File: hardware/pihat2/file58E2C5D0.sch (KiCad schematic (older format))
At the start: 43 parts, among them P1 USB_OTG, P2 BATT, P3 THERM, U1 MCP73833, U2 SMA_Edge_Mount, U3 SMA_Edge_Mount, U4 TPS61027, U5 MCP3021, U6 Si4464, X1 30MHz

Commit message: Worked on RF Layout.
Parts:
- removed C2: 10uF, Capacitors_SMD:C_0805, symbol C
- removed X1: 30MHz, Crystals:Crystal_SMD_5032_4Pads, symbol CRYSTAL_SMD
- added C10, C13: C, Capacitors_SMD:C_0805, symbol C
- added Y1: Crystal, Crystals:Crystal_HC49-SD_SMD, symbol Crystal
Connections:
- wire segments 164 -> 167

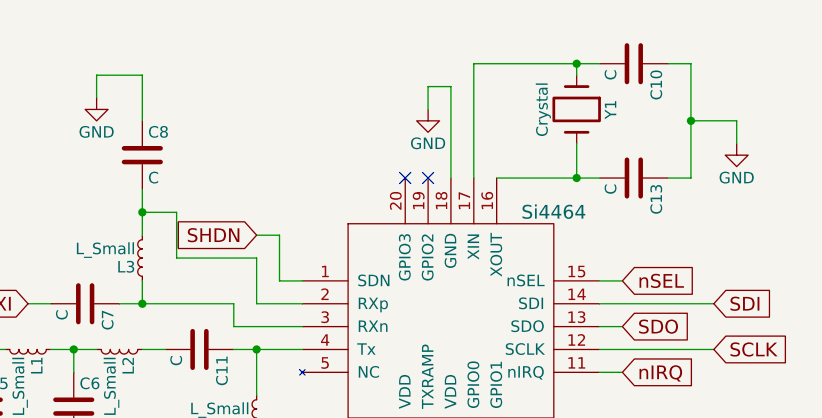
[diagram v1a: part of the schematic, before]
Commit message: Minor changes to pihat 2 in prep for boardhouse #2.
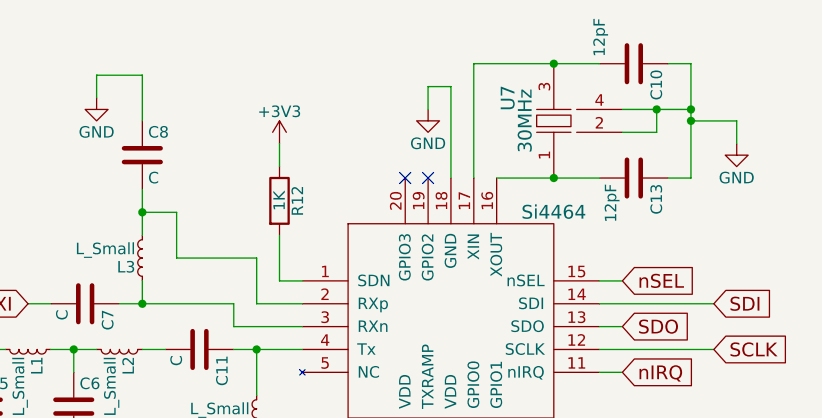
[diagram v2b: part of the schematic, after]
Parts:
- removed Y1: Crystal, Crystals:Crystal_HC49-SD_SMD, symbol Crystal
- added R12: 1K, Resistors_SMD:R_0805, symbol R
- added U7: 30MHz, Crystals:Crystal_SMD_Abracon_ABM3C-4pin_5.0x3.2mm, symbol AM3B_CRYSTAL
- C10, C13: value C -> 12pF
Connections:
- net labels removed: SHDN
- wire segments 167 -> 168
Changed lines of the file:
@@
 EESchema Schematic File Version 2
+LIBS:RPi_Hat-rescue
 LIBS:power
 LIBS:device
@@
 LIBS:contrib
 LIBS:valves
-LIBS:RFT
 LIBS:RPi_Hat-cache
 EELAYER 25 0
@@
 	9000 1600 9000 1400
 Wire Wire Line
-	9000 1400 8900 1400
-Text GLabel 8900 1400 0    60   Input ~ 0
-SHDN
-Wire Wire Line
 	9100 1900 8800 1900
 $Comp
@@
 	8200 4300 8200 4400
 $Comp
-L GND #PWR025
+L GND #PWR024
 U 1 1 58E2C8DB
 P 8200 4400
-F 0 "#PWR025" H 8200 4150 50  0001 C CNN
+F 0 "#PWR024" H 8200 4150 50  0001 C CNN
 F 1 "GND" H 8200 4250 50  0000 C CNN
 F 2 "" H 8200 4400 50  0000 C CNN
@@
 	9600 3300 9600 3400
 $Comp
-L GND #PWR026
+L GND #PWR025
 U 1 1 58E2C8DC
 P 9600 3400
-F 0 "#PWR026" H 9600 3150 50  0001 C CNN
+F 0 "#PWR025" H 9600 3150 50  0001 C CNN
 F 1 "GND" H 9600 3250 50  0000 C CNN
 F 2 "" H 9600 3400 50  0000 C CNN
@@
 	6950 3400 6950 3500
 $Comp
-L GND #PWR027
+L GND #PWR026
 U 1 1 58E2C8E0
 P 6950 3500
-F 0 "#PWR027" H 6950 3250 50  0001 C CNN
+F 0 "#PWR026" H 6950 3250 50  0001 C CNN
 F 1 "GND" H 6950 3350 50  0000 C CNN
 F 2 "" H 6950 3500 50  0000 C CNN
@@
 	7500 4600 7500 4700
 $Comp
-L GND #PWR028
+L GND #PWR027
 U 1 1 58E2C8E3
 P 7500 4700
-F 0 "#PWR028" H 7500 4450 50  0001 C CNN
+F 0 "#PWR027" H 7500 4450 50  0001 C CNN
 F 1 "GND" H 7500 4550 50  0000 C CNN
 F 2 "" H 7500 4700 50  0000 C CNN
@@
 	10550 3900 10550 4000
 $Comp
-L GND #PWR029
+L GND #PWR028
 U 1 1 58E2C8E5
 P 10550 4000
-F 0 "#PWR029" H 10550 3750 50  0001 C CNN
+F 0 "#PWR028" H 10550 3750 50  0001 C CNN
 F 1 "GND" H 10550 3850 50  0000 C CNN
 F 2 "" H 10550 4000 50  0000 C CNN
@@
 	10900 4400 10900 4500
 $Comp
-L GND #PWR030
+L GND #PWR029
 U 1 1 58E2C8E8
 P 10900 4500
-F 0 "#PWR030" H 10900 4250 50  0001 C CNN
+F 0 "#PWR029" H 10900 4250 50  0001 C CNN
 F 1 "GND" H 10900 4350 50  0000 C CNN
 F 2 "" H 10900 4500 50  0000 C CNN
@@
 Connection ~ 8650 5250
 $Comp
-L GND #PWR031
+L GND #PWR030
 U 1 1 58E2C8EB
 P 8650 5350
-F 0 "#PWR031" H 8650 5100 50  0001 C CNN
+F 0 "#PWR030" H 8650 5100 50  0001 C CNN
 F 1 "GND" H 8650 5200 50  0000 C CNN
 F 2 "" H 8650 5350 50  0000 C CNN
@@
 	8900 4750 8900 4650
 $Comp
-L +5V #PWR032
+L +5V #PWR031
 U 1 1 58E2C8EC
 P 8900 4650
-F 0 "#PWR032" H 8900 4500 50  0001 C CNN
+F 0 "#PWR031" H 8900 4500 50  0001 C CNN
 F 1 "+5V" H 8900 4790 50  0000 C CNN
 F 2 "" H 8900 4650 50  0000 C CNN
@@
 	6550 6550 6950 6550
 $Comp
-L +5V #PWR033
+L +5V #PWR032
 U 1 1 58E2C8F6
 P 1500 6150
-F 0 "#PWR033" H 1500 6000 50  0001 C CNN
+F 0 "#PWR032" H 1500 6000 50  0001 C CNN
 F 1 "+5V" H 1500 6290 50  0000 C CNN
 F 2 "" H 1500 6150 50  0000 C CNN
@@
 $EndComp
 $Comp
-L GND #PWR034
+L GND #PWR033
 U 1 1 58E2C8F7
 P 1500 6650
-F 0 "#PWR034" H 1500 6400 50  0001 C CNN
+F 0 "#PWR033" H 1500 6400 50  0001 C CNN
 F 1 "GND" H 1500 6500 50  0000 C CNN
 F 2 "" H 1500 6650 50  0000 C CNN
@@
 	3100 6500 3100 6600
 $Comp
-L GND #PWR035
+L GND #PWR034
 U 1 1 58E2C8F9
 P 3100 6600
-F 0 "#PWR035" H 3100 6350 50  0001 C CNN
+F 0 "#PWR034" H 3100 6350 50  0001 C CNN
 F 1 "GND" H 3100 6450 50  0000 C CNN
 F 2 "" H 3100 6600 50  0000 C CNN
@@
 Connection ~ 10550 2550
 $Comp
-L GND #PWR036
+L GND #PWR035
 U 1 1 58E2C901
 P 10650 2550
-F 0 "#PWR036" H 10650 2300 50  0001 C CNN
+F 0 "#PWR035" H 10650 2300 50  0001 C CNN
 F 1 "GND" H 10650 2400 50  0000 C CNN
 F 2 "" H 10650 2550 50  0000 C CNN
@@
 	2250 950  2250 850
 $Comp
-L +5V #PWR037
+L +5V #PWR036
 U 1 1 58E30706
 P 2250 850
-F 0 "#PWR037" H 2250 700 50  0001 C CNN
+F 0 "#PWR036" H 2250 700 50  0001 C CNN
 F 1 "+5V" H 2250 990 50  0000 C CNN
 F 2 "" H 2250 850 50  0000 C CNN
@@
 	2250 1850 2250 1950
 $Comp
-L GND #PWR038
+L GND #PWR037
 U 1 1 58E3098E
 P 2250 1950
-F 0 "#PWR038" H 2250 1700 50  0001 C CNN
+F 0 "#PWR037" H 2250 1700 50  0001 C CNN
 F 1 "GND" H 2250 1800 50  0000 C CNN
 F 2 "" H 2250 1950 50  0000 C CNN
@@
 VBATFILT
 $Comp
-L Crystal Y1
-U 1 1 58F13A4E
-P 10300 850
-F 0 "Y1" H 10300 1000 50  0000 C CNN
-F 1 "Crystal" H 10300 700 50  0000 C CNN
-F 2 "Crystals:Crystal_HC49-SD_SMD" H 10300 850 50  0001 C CNN
-F 3 "" H 10300 850 50  0000 C CNN
-	1    10300 850
-	0    1    1    0
-$EndComp
-Wire Wire Line
-	9850 650  10400 650
-Wire Wire Line
-	10300 650  10300 700
-Wire Wire Line
-	9950 1150 10400 1150
-Wire Wire Line
-	10300 1150 10300 1000
-$Comp
 L C C10
 U 1 1 58F142C3
 P 10550 650
 F 0 "C10" H 10575 750 50  0000 L CNN
-F 1 "C" H 10575 550 50  0000 L CNN
+F 1 "12pF" H 10350 500 50  0000 L CNN
 F 2 "Capacitors_SMD:C_0805" H 10588 500 50  0001 C CNN
 F 3 "" H 10550 650 50  0000 C CNN
@@
 	0    1    1    0
 $EndComp
-Connection ~ 10300 650
-Connection ~ 10300 1150
 $Comp
 L C C13
@@
 P 10550 1150
 F 0 "C13" H 10575 1250 50  0000 L CNN
-F 1 "C" H 10575 1050 50  0000 L CNN
+F 1 "12pF" H 10575 1050 50  0000 L CNN
 F 2 "Capacitors_SMD:C_0805" H 10588 1000 50  0001 C CNN
 F 3 "" H 10550 1150 50  0000 C CNN
@@
 Connection ~ 10800 900
 $Comp
-L GND #PWR039
+L GND #PWR038
 U 1 1 58F147CE
 P 11000 1000
-F 0 "#PWR039" H 11000 750 50  0001 C CNN
+F 0 "#PWR038" H 11000 750 50  0001 C CNN
 F 1 "GND" H 11000 850 50  0000 C CNN
 F 2 "" H 11000 1000 50  0000 C CNN
@@
 	1    0    0    -1
 $EndComp
+Wire Wire Line
+	10650 850  10650 950
+Wire Wire Line
+	10500 850  10800 850
+Connection ~ 10800 850
+$Comp
+L R R12
+U 1 1 59011587
+P 9000 1250
+F 0 "R12" V 9080 1250 50  0000 C CNN
+F 1 "1K" V 9000 1250 50  0000 C CNN
+F 2 "Resistors_SMD:R_0805" V 8930 1250 50  0001 C CNN
+F 3 "" H 9000 1250 50  0000 C CNN
+	1    9000 1250
+	1    0    0    -1
+$EndComp
+Wire Wire Line
+	9000 1100 9000 1000
+$Comp
+L +3V3 #PWR039
+U 1 1 59011701
+P 9000 1000
+F 0 "#PWR039" H 9000 850 50  0001 C CNN
+F 1 "+3V3" H 9000 1140 50  0000 C CNN
+F 2 "" H 9000 1000 50  0000 C CNN
+F 3 "" H 9000 1000 50  0000 C CNN
+	1    9000 1000
+	1    0    0    -1
+$EndComp
+$Comp
+L AM3B_CRYSTAL U7
+U 1 1 59011E68
+P 10200 900
+F 0 "U7" H 10300 1100 60  0000 C CNN
+F 1 "30MHz" H 10200 1025 60  0000 C CNN
+F 2 "Crystals:Crystal_SMD_Abracon_ABM3C-4pin_5.0x3.2mm" H 10200 900 60  0001 C CNN
+F 3 "" H 10200 900 60  0001 C CNN
+	1    10200 900
+	0    -1   -1   0
+$EndComp
+Wire Wire Line
+	9850 650  10400 650
+Connection ~ 10200 650
+Wire Wire Line
+	9950 1150 10400 1150
+Connection ~ 10200 1150
+Connection ~ 10650 850
+Wire Wire Line
+	10650 950  10500 950
 $EndSCHEMATC

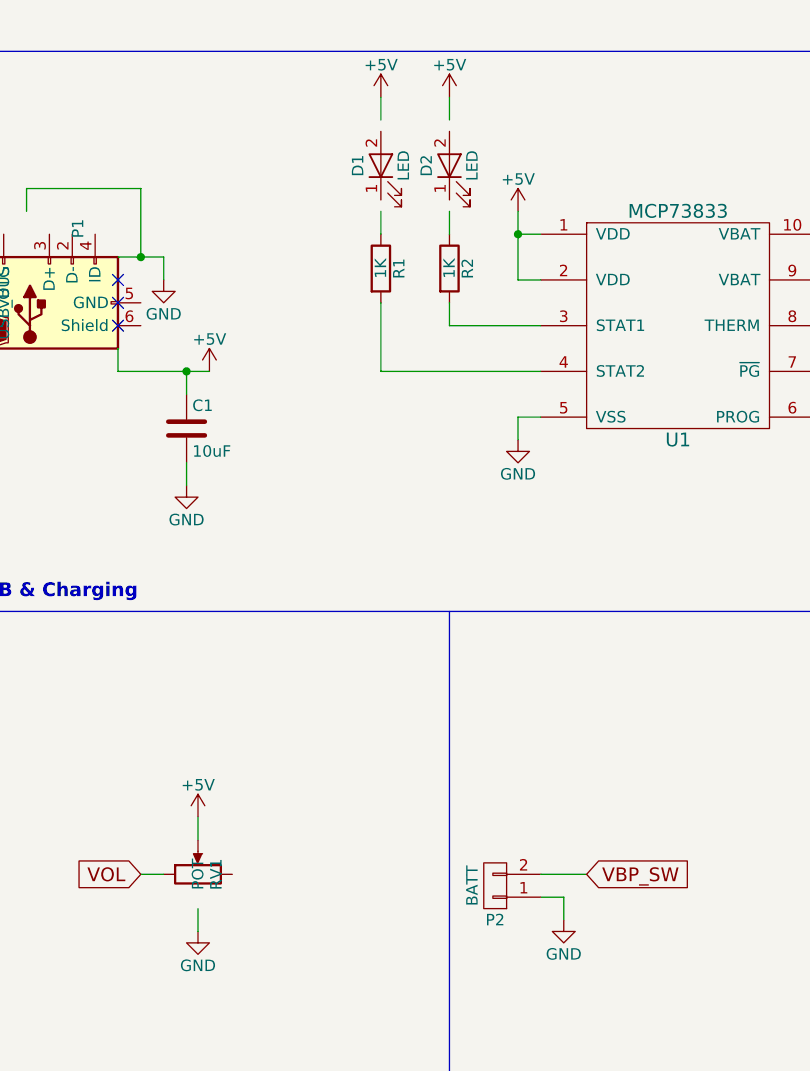
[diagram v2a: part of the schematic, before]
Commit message: Fixed issues with grounding and trace size.
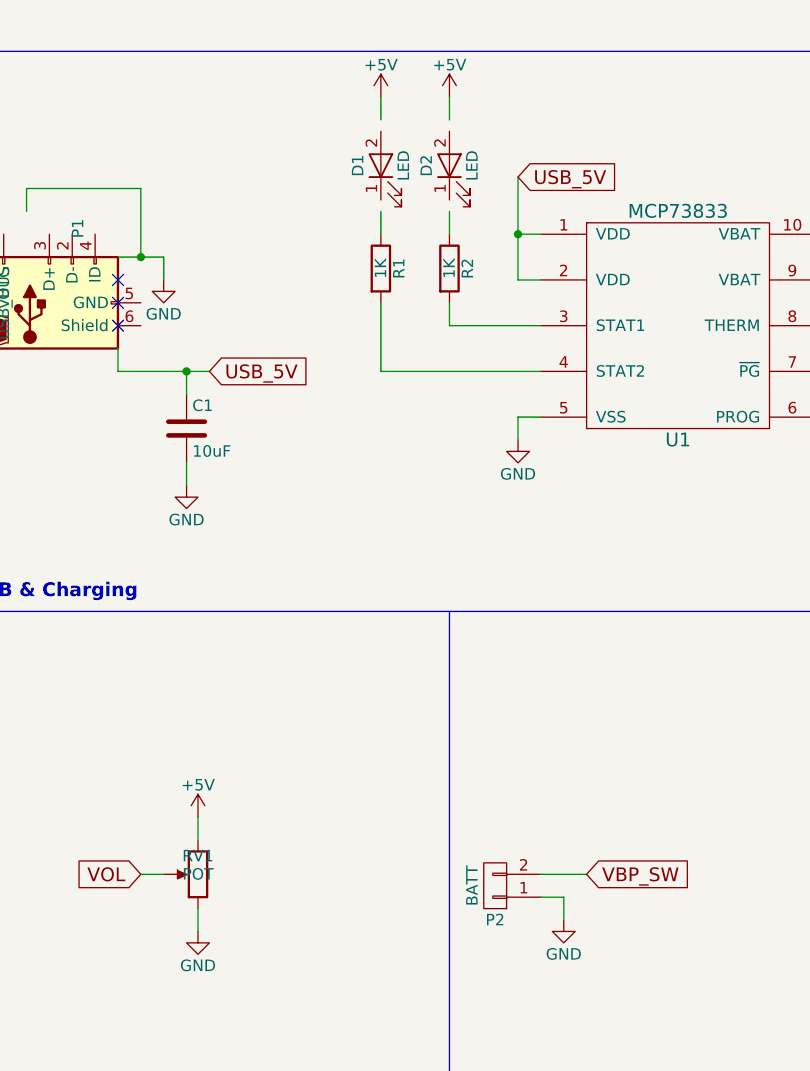
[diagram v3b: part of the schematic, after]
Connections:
- net labels added: USB_5V
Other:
- moved on the sheet: RV1
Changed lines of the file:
@@
 LIBS:contrib
 LIBS:valves
+LIBS:RFT
 LIBS:RPi_Hat-cache
 EELAYER 25 0
@@
 $EndComp
 Connection ~ 1450 4200
-$Comp
-L +5V #PWR016
-U 1 1 58E2C8C5
-P 1550 4200
-F 0 "#PWR016" H 1550 4050 50  0001 C CNN
-F 1 "+5V" H 1550 4340 50  0000 C CNN
-F 2 "" H 1550 4200 50  0000 C CNN
-F 3 "" H 1550 4200 50  0000 C CNN
-	1    1550 4200
-	1    0    0    -1
-$EndComp
 Wire Bus Line
 	500  2800 4300 2800
@@
 $EndComp
 Wire Wire Line
-	3000 3800 2900 3800
-Wire Wire Line
-	2900 3800 2900 3500
+	2900 3800 3000 3800
+Wire Wire Line
+	2900 3350 2900 3800
 Wire Wire Line
 	3000 3600 2900 3600
 Connection ~ 2900 3600
 $Comp
-L +5V #PWR017
-U 1 1 58E2C8C7
-P 2900 3500
-F 0 "#PWR017" H 2900 3350 50  0001 C CNN
-F 1 "+5V" H 2900 3640 50  0000 C CNN
-F 2 "" H 2900 3500 50  0000 C CNN
-F 3 "" H 2900 3500 50  0000 C CNN
-	1    2900 3500
-	1    0    0    -1
-$EndComp
-$Comp
-L +5V #PWR018
+L +5V #PWR016
 U 1 1 58E2C8C8
 P 2600 3000
-F 0 "#PWR018" H 2600 2850 50  0001 C CNN
+F 0 "#PWR016" H 2600 2850 50  0001 C CNN
 F 1 "+5V" H 2600 3140 50  0000 C CNN
 F 2 "" H 2600 3000 50  0000 C CNN
@@
 $EndComp
 $Comp
-L +5V #PWR019
+L +5V #PWR017
 U 1 1 58E2C8C9
 P 2300 3000
-F 0 "#PWR019" H 2300 2850 50  0001 C CNN
+F 0 "#PWR017" H 2300 2850 50  0001 C CNN
 F 1 "+5V" H 2300 3140 50  0000 C CNN
 F 2 "" H 2300 3000 50  0000 C CNN
@@
 U 1 1 58E2C8CB
 P 2600 3300
+AR Path="/58E2C8CB" Ref="D2"  Part="1"
+AR Path="/5515D395/58E2C5D1/58E2C8CB" Ref="D2"  Part="1"
 F 0 "D2" H 2600 3400 50  0000 C CNN
 F 1 "LED" H 2600 3200 50  0000 C CNN
@@
 U 1 1 58E2C8CD
 P 2300 3300
+AR Path="/58E2C8CD" Ref="D1"  Part="1"
+AR Path="/5515D395/58E2C5D1/58E2C8CD" Ref="D1"  Part="1"
 F 0 "D1" H 2300 3400 50  0000 C CNN
 F 1 "LED" H 2300 3200 50  0000 C CNN
@@
 	2900 4400 2900 4500
 $Comp
-L GND #PWR020
+L GND #PWR018
 U 1 1 58E2C8CE
 P 2900 4500
-F 0 "#PWR020" H 2900 4250 50  0001 C CNN
+F 0 "#PWR018" H 2900 4250 50  0001 C CNN
 F 1 "GND" H 2900 4350 50  0000 C CNN
 F 2 "" H 2900 4500 50  0000 C CNN
@@
 	4300 4800 4300 4900
 $Comp
-L GND #PWR021
+L GND #PWR019
 U 1 1 58E2C8D0
 P 4300 4900
-F 0 "#PWR021" H 4300 4650 50  0001 C CNN
+F 0 "#PWR019" H 4300 4650 50  0001 C CNN
 F 1 "GND" H 4300 4750 50  0000 C CNN
 F 2 "" H 4300 4900 50  0000 C CNN
@@
 U 1 1 58E2C8D2
 P 4600 2800
+AR Path="/58E2C8D2" Ref="D3"  Part="1"
+AR Path="/5515D395/58E2C5D1/58E2C8D2" Ref="D3"  Part="1"
 F 0 "D3" H 4600 2900 50  0000 C CNN
 F 1 "LED" H 4600 2700 50  0000 C CNN
@@
 $EndComp
 $Comp
-L +5V #PWR022
+L +5V #PWR020
 U 1 1 58E2C8D3
 P 4600 2500
-F 0 "#PWR022" H 4600 2350 50  0001 C CNN
+F 0 "#PWR020" H 4600 2350 50  0001 C CNN
 F 1 "+5V" H 4600 2640 50  0000 C CNN
 F 2 "" H 4600 2500 50  0000 C CNN
@@
 Connection ~ 5200 4900
 $Comp
-L GND #PWR023
+L GND #PWR021
 U 1 1 58E2C8D7
 P 5200 5000
-F 0 "#PWR023" H 5200 4750 50  0001 C CNN
+F 0 "#PWR021" H 5200 4750 50  0001 C CNN
 F 1 "GND" H 5200 4850 50  0000 C CNN
 F 2 "" H 5200 5000 50  0000 C CNN
@@
 	8200 4300 8200 4400
 $Comp
-L GND #PWR024
+L GND #PWR022
 U 1 1 58E2C8DB
 P 8200 4400
-F 0 "#PWR024" H 8200 4150 50  0001 C CNN
+F 0 "#PWR022" H 8200 4150 50  0001 C CNN
 F 1 "GND" H 8200 4250 50  0000 C CNN
 F 2 "" H 8200 4400 50  0000 C CNN
@@
 	9600 3300 9600 3400
 $Comp
-L GND #PWR025
+L GND #PWR023
 U 1 1 58E2C8DC
 P 9600 3400
-F 0 "#PWR025" H 9600 3150 50  0001 C CNN
+F 0 "#PWR023" H 9600 3150 50  0001 C CNN
 F 1 "GND" H 9600 3250 50  0000 C CNN
 F 2 "" H 9600 3400 50  0000 C CNN
@@
 	6950 3400 6950 3500
 $Comp
-L GND #PWR026
+L GND #PWR024
 U 1 1 58E2C8E0
 P 6950 3500
-F 0 "#PWR026" H 6950 3250 50  0001 C CNN
+F 0 "#PWR024" H 6950 3250 50  0001 C CNN
 F 1 "GND" H 6950 3350 50  0000 C CNN
 F 2 "" H 6950 3500 50  0000 C CNN
@@
 Wire Wire Line
 	7400 3700 8300 3700
-$Comp
-L R R7
-U 1 1 58E2C8E1
-P 7500 3950
-F 0 "R7" V 7580 3950 50  0000 C CNN
-F 1 "R" V 7500 3950 50  0000 C CNN
-F 2 "Resistors_SMD:R_0603" V 7430 3950 50  0001 C CNN
-F 3 "" H 7500 3950 50  0000 C CNN
-	1    7500 3950
-	1    0    0    -1
-$EndComp
 $Comp
 L R R8
@@
 	7500 4600 7500 4700
 $Comp
-L GND #PWR027
+L GND #PWR025
 U 1 1 58E2C8E3
 P 7500 4700
-F 0 "#PWR027" H 7500 4450 50  0001 C CNN
+F 0 "#PWR025" H 7500 4450 50  0001 C CNN
 F 1 "GND" H 7500 4550 50  0000 C CNN
 F 2 "" H 7500 4700 50  0000 C CNN
@@
 	10550 3900 10550 4000
 $Comp
-L GND #PWR028
+L GND #PWR026
 U 1 1 58E2C8E5
 P 10550 4000
-F 0 "#PWR028" H 10550 3750 50  0001 C CNN
+F 0 "#PWR026" H 10550 3750 50  0001 C CNN
 F 1 "GND" H 10550 3850 50  0000 C CNN
 F 2 "" H 10550 4000 50  0000 C CNN
@@
 	10900 4400 10900 4500
 $Comp
-L GND #PWR029
+L GND #PWR027
 U 1 1 58E2C8E8
 P 10900 4500
-F 0 "#PWR029" H 10900 4250 50  0001 C CNN
+F 0 "#PWR027" H 10900 4250 50  0001 C CNN
 F 1 "GND" H 10900 4350 50  0000 C CNN
 F 2 "" H 10900 4500 50  0000 C CNN
@@
 Connection ~ 8650 5250
 $Comp
-L GND #PWR030
+L GND #PWR028
 U 1 1 58E2C8EB
 P 8650 5350
-F 0 "#PWR030" H 8650 5100 50  0001 C CNN
+F 0 "#PWR028" H 8650 5100 50  0001 C CNN
 F 1 "GND" H 8650 5200 50  0000 C CNN
 F 2 "" H 8650 5350 50  0000 C CNN
@@
 	8900 4750 8900 4650
 $Comp
-L +5V #PWR031
+L +5V #PWR029
 U 1 1 58E2C8EC
 P 8900 4650
-F 0 "#PWR031" H 8900 4500 50  0001 C CNN
+F 0 "#PWR029" H 8900 4500 50  0001 C CNN
 F 1 "+5V" H 8900 4790 50  0000 C CNN
 F 2 "" H 8900 4650 50  0000 C CNN
@@
 	6550 6550 6950 6550
 $Comp
-L +5V #PWR032
+L +5V #PWR030
 U 1 1 58E2C8F6
 P 1500 6150
-F 0 "#PWR032" H 1500 6000 50  0001 C CNN
+F 0 "#PWR030" H 1500 6000 50  0001 C CNN
 F 1 "+5V" H 1500 6290 50  0000 C CNN
 F 2 "" H 1500 6150 50  0000 C CNN
@@
 $EndComp
 $Comp
-L GND #PWR033
+L GND #PWR031
 U 1 1 58E2C8F7
 P 1500 6650
-F 0 "#PWR033" H 1500 6400 50  0001 C CNN
+F 0 "#PWR031" H 1500 6400 50  0001 C CNN
 F 1 "GND" H 1500 6500 50  0000 C CNN
 F 2 "" H 1500 6650 50  0000 C CNN
@@
 	3100 6500 3100 6600
 $Comp
-L GND #PWR034
+L GND #PWR032
 U 1 1 58E2C8F9
 P 3100 6600
-F 0 "#PWR034" H 3100 6350 50  0001 C CNN
+F 0 "#PWR032" H 3100 6350 50  0001 C CNN
 F 1 "GND" H 3100 6450 50  0000 C CNN
 F 2 "" H 3100 6600 50  0000 C CNN
@@
 F 3 "" H 1500 6400 50  0000 C CNN
 	1    1500 6400
-	0    -1   -1   0
+	-1   0    0    1
 $EndComp
 $Comp
@@
 Connection ~ 10550 2550
 $Comp
-L GND #PWR035
+L GND #PWR033
 U 1 1 58E2C901
 P 10650 2550
-F 0 "#PWR035" H 10650 2300 50  0001 C CNN
+F 0 "#PWR033" H 10650 2300 50  0001 C CNN
 F 1 "GND" H 10650 2400 50  0000 C CNN
 F 2 "" H 10650 2550 50  0000 C CNN
@@
 	2250 950  2250 850
 $Comp
-L +5V #PWR036
+L +5V #PWR034
 U 1 1 58E30706
 P 2250 850
-F 0 "#PWR036" H 2250 700 50  0001 C CNN
+F 0 "#PWR034" H 2250 700 50  0001 C CNN
 F 1 "+5V" H 2250 990 50  0000 C CNN
 F 2 "" H 2250 850 50  0000 C CNN
@@
 	2250 1850 2250 1950
 $Comp
-L GND #PWR037
+L GND #PWR035
 U 1 1 58E3098E
 P 2250 1950
-F 0 "#PWR037" H 2250 1700 50  0001 C CNN
+F 0 "#PWR035" H 2250 1700 50  0001 C CNN
 F 1 "GND" H 2250 1800 50  0000 C CNN
 F 2 "" H 2250 1950 50  0000 C CNN
@@
 Connection ~ 10800 900
 $Comp
-L GND #PWR038
+L GND #PWR036
 U 1 1 58F147CE
 P 11000 1000
-F 0 "#PWR038" H 11000 750 50  0001 C CNN
+F 0 "#PWR036" H 11000 750 50  0001 C CNN
 F 1 "GND" H 11000 850 50  0000 C CNN
 F 2 "" H 11000 1000 50  0000 C CNN
@@
 	9000 1100 9000 1000
 $Comp
-L +3V3 #PWR039
+L +3V3 #PWR037
 U 1 1 59011701
 P 9000 1000
-F 0 "#PWR039" H 9000 850 50  0001 C CNN
+F 0 "#PWR037" H 9000 850 50  0001 C CNN
 F 1 "+3V3" H 9000 1140 50  0000 C CNN
 F 2 "" H 9000 1000 50  0000 C CNN
@@
 Wire Wire Line
 	10650 950  10500 950
+$Comp
+L R R7
+U 1 1 58E2C8E1
+P 7500 3950
+F 0 "R7" V 7580 3950 50  0000 C CNN
+F 1 "R" V 7500 3950 50  0000 C CNN
+F 2 "Resistors_SMD:R_0603" V 7430 3950 50  0001 C CNN
+F 3 "" H 7500 3950 50  0000 C CNN
+	1    7500 3950
+	1    0    0    -1
+$EndComp
+Text GLabel 2900 3350 2    60   Input ~ 0
+USB_5V
+Text GLabel 1550 4200 2    60   Input ~ 0
+USB_5V
 $EndSCHEMATC
